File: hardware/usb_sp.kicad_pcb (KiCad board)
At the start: 4 copper layers, 38.1 x 59.7 mm, 48 parts, among them U1 CH32V203C8U6, U10 SN74LVC1G32DBVR, U2 ZD24C02B-MAGMT, U3 32.768kHz, U4 KH-TYPE-C-16P, U5 SD101CWS, U6 CH572D, U7 HX_JN1_27-2X5P_ZZ_H4_9, U8 HX_JN1_27-2X5P_ZZ_H4_9, U9 SN74LVC1G32DBVR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

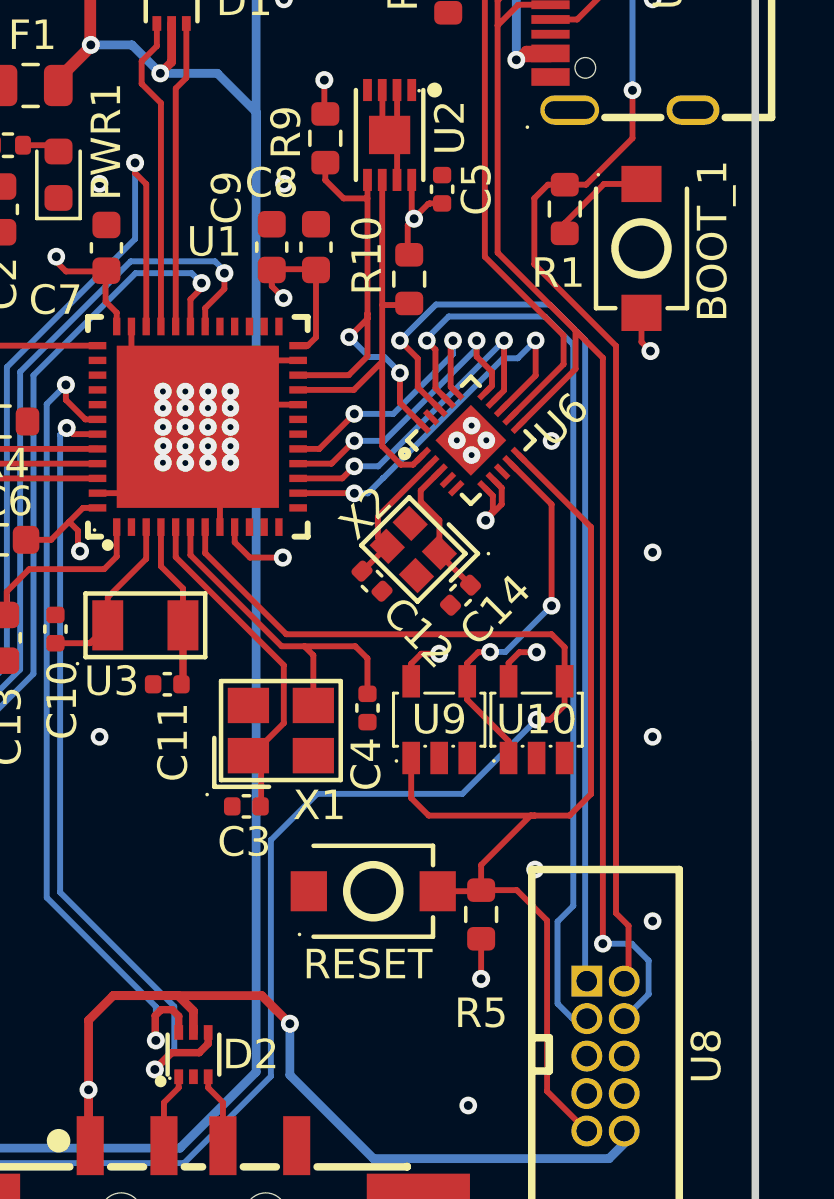
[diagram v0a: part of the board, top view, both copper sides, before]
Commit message: add developemnt board and fix issue related to dual i2c access
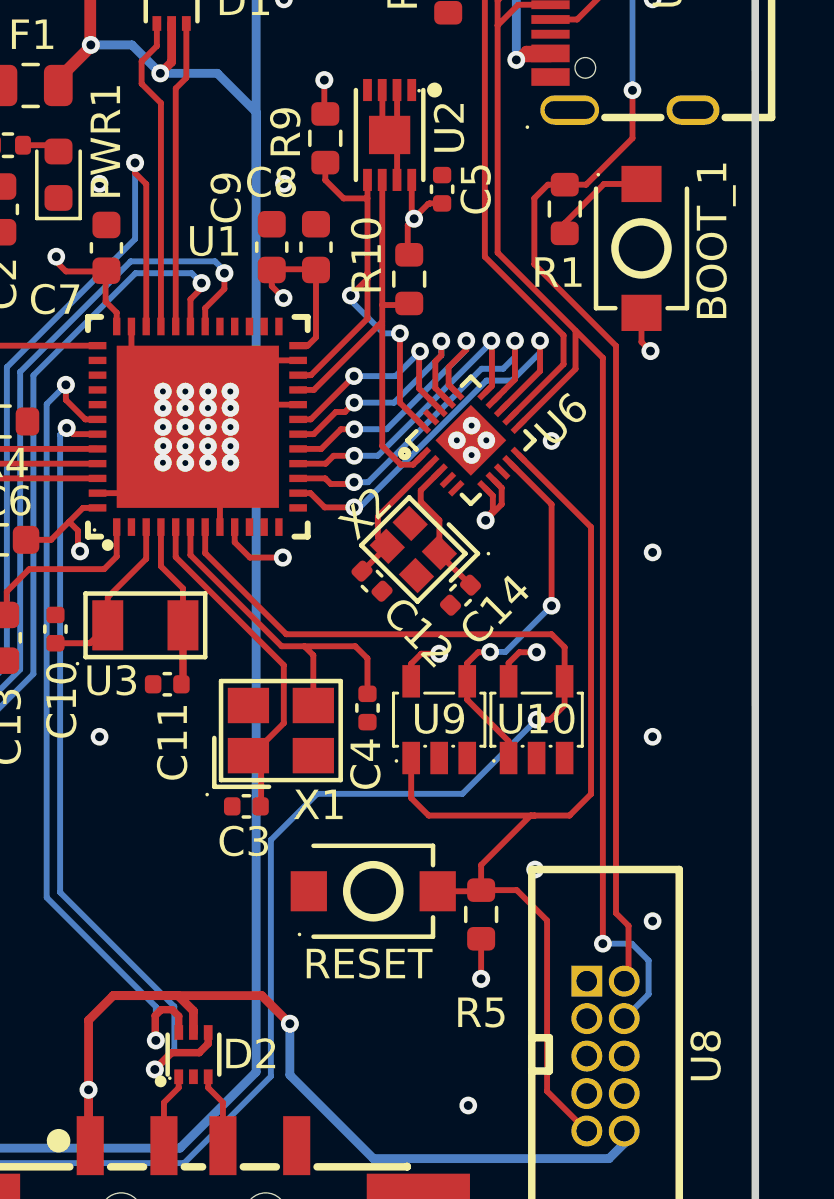
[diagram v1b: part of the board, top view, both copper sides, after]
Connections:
- U1 pad 18: unconnected-(U1-PB0/ADC8-Pad18) -> /CH32V203/GPIO_I2C_CTRL
- U1 pad 19: unconnected-(U1-PB1/ADC9-Pad19) -> /CH32V203/GPIO_RESERVED_1
- U6 pad 17: /CH572D/UART_RX -> /CH32V203/GPIO_I2C_CTRL
- U6 pad 18: /CH572D/UART_TX -> /CH32V203/GPIO_RESERVED_1
- U8 pad 1: /CH572D/UART_TX -> unconnected-(U8-Pad1)
- U8 pad 3: /CH572D/UART_RX -> unconnected-(U8-Pad3)
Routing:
- net /CH572D/UART_TX: track 31.9 -> 0.00 mm, vias 1 -> 0
- net /CH572D/UART_RX: track 31.8 -> 0.00 mm, vias 1 -> 0
- net /CH32V203/GPIO_I2C_CTRL: track 0.00 -> 8.92 mm, vias 0 -> 2
- net /CH32V203/GPIO_RESERVED_1: track 0.00 -> 7.49 mm, vias 0 -> 2
- net /CH32V203/SPI_CLK: track 11.1 -> 12.1 mm
- net /CH32V203/SPI_CS: track 13.2 -> 13.8 mm
- net /CH32V203/EEPROM_SDA: track 16.3 -> 16.9 mm
- net /CH32V203/SPI_MOSI: track 8.91 -> 9.50 mm
- net /CH32V203/EEPROM_SCL: track 15.0 -> 15.5 mm
